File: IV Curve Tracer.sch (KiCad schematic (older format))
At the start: 61 parts, among them IC1 MAX680ESA+, J0 TB002-500-02BE, J1 CAN_Out, J5 Conn_01x15, J6 Conn_01x15, Q1 IRF100P218XKMA1, Q2 IRF100P218XKMA1, SW0 SW_Rotary2x3, U1 INA211CQDCKRQ1, U2 LT1215, U3 LT1215, U4 ADM3055E, U5 CDSOT23-T24CAN

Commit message: CAN updated, needs bugfixes and footprint review.
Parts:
- added C18, C3: .1uF, Capacitor_SMD:C_0402_1005Metric, symbol IV-Curve-Tracer-rescue:SMDTC04100TA00JS00-SamacSys_Parts-IV-Curve-Tracer-rescue
- added J7: CAN_In, TerminalBlock_Phoenix:TerminalBlock_Phoenix_MKDS-1,5-4_1x04_P5.00mm_Horizontal, symbol Connector:Screw_Terminal_01x04
- added TP10: CAN_Rx, TestPoint:TestPoint_Keystone_5005-5009_Compact, symbol Connector:TestPoint
- added TP11: CAN_Tx, TestPoint:TestPoint_Keystone_5005-5009_Compact, symbol Connector:TestPoint
- added TP12: GroundTP, TestPoint:TestPoint_Keystone_5005-5009_Compact, symbol Connector:TestPoint
- added TP6: ISO_Vout, TestPoint:TestPoint_Keystone_5005-5009_Compact, symbol Connector:TestPoint
- added TP7: ISO_Vin, TestPoint:TestPoint_Keystone_5005-5009_Compact, symbol Connector:TestPoint
- added TP8: ISO_GNDout, TestPoint:TestPoint_Keystone_5005-5009_Compact, symbol Connector:TestPoint
- added TP9: ISO_GNDin, TestPoint:TestPoint_Keystone_5005-5009_Compact, symbol Connector:TestPoint
- C14, C15, C16, C17: symbol IV-Curve-Tracer-rescue:HMK325C7475KM-PE-SamacSys_Parts -> IV-Curve-Tracer-rescue:HMK325C7475KM-PE-SamacSys_Parts-IV-Curve-Tracer-rescue
- C2, C4, C5: symbol IV-Curve-Tracer-rescue:SMDTC04100TA00JS00-SamacSys_Parts -> IV-Curve-Tracer-rescue:SMDTC04100TA00JS00-SamacSys_Parts-IV-Curve-Tracer-rescue
- IC1: symbol IV-Curve-Tracer-rescue:MAX680ESA+-SamacSys_Parts -> IV-Curve-Tracer-rescue:MAX680ESA+-SamacSys_Parts-IV-Curve-Tracer-rescue
- LED1, LED2, LED3, LED4: symbol IV-Curve-Tracer-rescue:TLHR5400-AS12Z-SamacSys_Parts -> IV-Curve-Tracer-rescue:TLHR5400-AS12Z-SamacSys_Parts-IV-Curve-Tracer-rescue
- SW0: symbol IV-Curve-Tracer-rescue:SW_Rotary2x3-Switch -> IV-Curve-Tracer-rescue:SW_Rotary2x3-Switch-IV-Curve-Tracer-rescue
- U4: symbol IV-Curve-Tracer-rescue:ADM3055EBRIZ-SamacSys_Parts -> IV-Curve-Tracer-rescue:ADM3055EBRIZ-SamacSys_Parts-IV-Curve-Tracer-rescue
- U5: footprint SamacSys_Parts:SOT95P230X117-3N -> Package_TO_SOT_SMD:SOT-23W_Handsoldering; symbol IV-Curve-Tracer-rescue:CDSOT23-T24CAN-SamacSys_Parts -> IV-Curve-Tracer-rescue:CDSOT23-T24CAN-SamacSys_Parts-IV-Curve-Tracer-rescue
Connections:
- wire segments 189 -> 207
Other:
- moved on the sheet: C7, C8, C9

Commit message: proof checked, drc run and mounting holes added.
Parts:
- added H1, H2, H3, H4: MountingHole, MountingHole:MountingHole_3.2mm_M3, symbol Mechanical:MountingHole
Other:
- note added: "CAN Circuit"
- note removed: "* Make a custom \nfootprint for this"

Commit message: moved ADC_V pin down two
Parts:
- J1, J7: footprint TerminalBlock_Phoenix:TerminalBlock_Phoenix_MKDS-1,5-4_1x04_P5.00mm_Horizontal -> Connector_Molex:Molex_Micro-Fit_3.0_43650-0415_1x04_P3.00mm_Vertical
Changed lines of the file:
@@
 	-1   0    0    -1
 $EndComp
-Text GLabel 10900 3900 2    50   Input ~ 0
+Text GLabel 10900 4100 2    50   Input ~ 0
 ADC_V
 Wire Wire Line
@@
 NoConn ~ 10500 4400
 NoConn ~ 10500 4300
-NoConn ~ 10500 4100
+NoConn ~ 10500 3900
 NoConn ~ 10500 3700
 Text Notes 7000 6800 0    50   ~ 0
@@
 	1    0    0    -1
 $EndComp
+$Comp
+L Device:R R8
+U 1 1 5EF5A814
+P 1700 2450
+F 0 "R8" H 1770 2496 50  0000 L CNN
+F 1 "2k" H 1770 2405 50  0000 L CNN
+F 2 "Resistor_THT:R_Axial_DIN0204_L3.6mm_D1.6mm_P5.08mm_Vertical" V 1630 2450 50  0001 C CNN
+F 3 "~" H 1700 2450 50  0001 C CNN
+	1    1700 2450
+	1    0    0    -1
+$EndComp
+Connection ~ 1700 2300
 Connection ~ 1350 2200
 Wire Wire Line
@@
 F 0 "J1" H 8000 5800 60  0000 C CNN
 F 1 "CAN_Out" H 7900 6100 60  0000 C CNN
-F 2 "TerminalBlock_Phoenix:TerminalBlock_Phoenix_MKDS-1,5-4_1x04_P5.00mm_Horizontal" H 8050 6150 60  0001 C CNN
+F 2 "Connector_Molex:Molex_Micro-Fit_3.0_43650-0415_1x04_P3.00mm_Vertical" H 8050 6150 60  0001 C CNN
 F 3 "https://www.mouser.com/datasheet/2/324/3/ItemDetail_1718605-916253.pdf" H 8050 6150 60  0001 C CNN
 	1    7900 5850
@@
 F 0 "J7" H 8000 5200 60  0000 C CNN
 F 1 "CAN_In" H 7900 5500 60  0000 C CNN
-F 2 "TerminalBlock_Phoenix:TerminalBlock_Phoenix_MKDS-1,5-4_1x04_P5.00mm_Horizontal" H 8050 5550 60  0001 C CNN
+F 2 "Connector_Molex:Molex_Micro-Fit_3.0_43650-0415_1x04_P3.00mm_Vertical" H 8050 5550 60  0001 C CNN
 F 3 "https://www.mouser.com/datasheet/2/324/3/ItemDetail_1718605-916253.pdf" H 8050 5550 60  0001 C CNN
 	1    7900 5250
@@
 	10850 4300 10850 3800
 Wire Wire Line
-	10500 3900 10900 3900
+	10500 4100 10900 4100
 Wire Wire Line
 	10500 4000 10900 4000
@@
 Text Notes 850  4700 0    50   ~ 0
 CAN Circuit
-Connection ~ 1700 2300
-$Comp
-L Device:R R8
-U 1 1 5EF5A814
-P 1700 2450
-F 0 "R8" H 1770 2496 50  0000 L CNN
-F 1 "2k" H 1770 2405 50  0000 L CNN
-F 2 "Resistor_THT:R_Axial_DIN0204_L3.6mm_D1.6mm_P5.08mm_Vertical" V 1630 2450 50  0001 C CNN
-F 3 "~" H 1700 2450 50  0001 C CNN
-	1    1700 2450
-	1    0    0    -1
-$EndComp
 $EndSCHEMATC

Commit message: Major Curve Tracer Board overhaul. Schematic advanced to Rev 1.1.0. Layout advanced to Rev 1.1.0. Parts list advanced to Rev 1.1.0.
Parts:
- removed C1: Variable, Capacitor_SMD:C_0805_2012Metric, symbol Device:C
- removed C14, C16, C17: 4.7uF, Capacitor_SMD:C_1210_3225Metric, symbol IV-Curve-Tracer-rescue:HMK325C7475KM-PE-SamacSys_Parts-IV-Curve-Tracer-rescue
- removed C18, C2, C3: .1uF, Capacitor_SMD:C_0402_1005Metric, symbol IV-Curve-Tracer-rescue:SMDTC04100TA00JS00-SamacSys_Parts-IV-Curve-Tracer-rescue
- removed J1: CAN_Out, Connector_Molex:Molex_Micro-Fit_3.0_43650-0415_1x04_P3.00mm_Vertical, symbol Connector:Screw_Terminal_01x04
- removed J5, J6: Conn_01x15, Connector_PinHeader_2.54mm:PinHeader_1x15_P2.54mm_Vertical, symbol Connector_Generic:Conn_01x15
- removed J7: CAN_In, Connector_Molex:Molex_Micro-Fit_3.0_43650-0415_1x04_P3.00mm_Vertical, symbol Connector:Screw_Terminal_01x04
- removed JP1: Termination Resistors, Connector_PinHeader_2.54mm:PinHeader_1x02_P2.54mm_Vertical, symbol Device:Jumper_NC_Small
- removed LED2, LED3, LED4: TLHR5400-AS12Z, LED_THT:LED_D3.0mm, symbol IV-Curve-Tracer-rescue:TLHR5400-AS12Z-SamacSys_Parts-IV-Curve-Tracer-rescue
- removed R10, R9: 330, Resistor_THT:R_Axial_DIN0204_L3.6mm_D1.6mm_P5.08mm_Vertical, symbol Device:R
- removed R11: 1k, Resistor_THT:R_Axial_DIN0204_L3.6mm_D1.6mm_P5.08mm_Vertical, symbol Device:R
- removed R12: 0, Resistor_SMD:R_0805_2012Metric, symbol Device:R
- removed R14, R15: 60, Resistor_SMD:R_0805_2012Metric, symbol Device:R
- removed TP4: CAN_H, TestPoint:TestPoint_Keystone_5005-5009_Compact, symbol Connector:TestPoint
- removed TP5: CAN_L, TestPoint:TestPoint_Keystone_5005-5009_Compact, symbol Connector:TestPoint
- removed TP6: ISO_Vout, TestPoint:TestPoint_Keystone_5005-5009_Compact, symbol Connector:TestPoint
- removed U5: CDSOT23-T24CAN, Package_TO_SOT_SMD:SOT-23W_Handsoldering, symbol IV-Curve-Tracer-rescue:CDSOT23-T24CAN-SamacSys_Parts-IV-Curve-Tracer-rescue
- added C0, C15: .1uF, Capacitor_SMD:C_0805_2012Metric, symbol Device:C_Small
- added C14: 10uF, Capacitor_SMD:C_0805_2012Metric, symbol Device:C_Small
- added C16, CA_2, CB_2, CC_2: .01uF, Capacitor_SMD:C_0805_2012Metric, symbol Device:C_Small
- added C5: 4.7uF, Capacitor_SMD:C_0805_2012Metric, symbol Device:C_Small
- added F1: Fuse, IV Curve Tracer:05200101Z_Fuze_Holder_5x20_PCB_Mount, symbol Device:Fuse
- added J0: 9V Supply, Connector_Molex:Molex_Micro-Fit_3.0_43650-0215_1x02_P3.00mm_Vertical, symbol Connector_Generic:Conn_01x02
- added J2: CAN_In, Connector_Molex:Molex_Micro-Fit_3.0_43650-0415_1x04_P3.00mm_Vertical, symbol Array:CAN_Connector_43650-0427
- added J3: CAN_Out, Connector_Molex:Molex_Micro-Fit_3.0_43650-0415_1x04_P3.00mm_Vertical, symbol Array:CAN_Connector_43650-0427
- added JP1: Termination Resistors, Connector_PinHeader_2.54mm:PinHeader_1x02_P2.54mm_Vertical, symbol Device:Jumper_NO_Small
- added LED2: Scanning (Blue), LED_SMD:LED_0805_2012Metric, symbol Device:LED_ALT
- added LED3: CAN_Rx (Blue), LED_SMD:LED_0805_2012Metric, symbol Device:LED_ALT
- added LED4: CAN_Tx (Blue), LED_SMD:LED_0805_2012Metric, symbol Device:LED_ALT
- added LED5: Error (Amber), LED_SMD:LED_0805_2012Metric, symbol Device:LED_ALT
- added R1, R2, R3, R5: 330, Resistor_SMD:R_0805_2012Metric, symbol Device:R
- added R16: 0, Resistor_SMD:R_0805_2012Metric, symbol Device:R_Small
- added R17, R18: 60, Resistor_SMD:R_0805_2012Metric, symbol Device:R_Small
- added SW1: SW_Push, Button_Switch_THT:SW_PUSH_6mm, symbol Switch:SW_Push
- added TP1: GND, TestPoint:TestPoint_Keystone_5005-5009_Compact, symbol Connector:TestPoint
- added TP12: CAN_ISO_GndOut, TestPoint:TestPoint_Keystone_5005-5009_Compact, symbol Connector:TestPoint
- added TP13: CAN_H, TestPoint:TestPoint_Keystone_5005-5009_Compact, symbol Connector:TestPoint
- added TP14: CAN_L, TestPoint:TestPoint_Keystone_5005-5009_Compact, symbol Connector:TestPoint
- added U1: MCU_Nucleo_L432KC, IV Curve Tracer:MODULE_NUCLEO-L432KC, symbol Array:MCU_Nucleo_L432KC
- added U7: CDSOT23-T24CAN, Package_TO_SOT_SMD:SOT-23, symbol Array:CAN_Bus_Protector_CDSOT23-T24CAN
- C1: renamed from C4; footprint Capacitor_SMD:C_0402_1005Metric -> Capacitor_SMD:C_0805_2012Metric; symbol IV-Curve-Tracer-rescue:SMDTC04100TA00JS00-SamacSys_Parts-IV-Curve-Tracer-rescue -> Device:C_Small; Description CGA2B1X7R1C104K050BC - Multilayer Ceramic Capacitors MLCC -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 -> (none)
- C10: value 0.22uF -> .1uF
- C11: value 10uF -> .1uF
- C12: value 0.1uF -> .01uF
- C13: value 0.01uF -> .22uF
- C3: renamed from C5; footprint Capacitor_SMD:C_0402_1005Metric -> Capacitor_SMD:C_0805_2012Metric; symbol IV-Curve-Tracer-rescue:SMDTC04100TA00JS00-SamacSys_Parts-IV-Curve-Tracer-rescue -> Device:C_Small; Description CGA2B1X7R1C104K050BC - Multilayer Ceramic Capacitors MLCC -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 -> (none)
- C4: renamed from C15; footprint Capacitor_SMD:C_1210_3225Metric -> Capacitor_SMD:C_0805_2012Metric; symbol IV-Curve-Tracer-rescue:HMK325C7475KM-PE-SamacSys_Parts-IV-Curve-Tracer-rescue -> Device:C_Small; Description HMK325C7475KM-PE - Multilayer Ceramic Capacitors MLCC - SMD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 -> (none)
- C6: value 10uF -> 4.7uF; Height (none) -> 2.7; Manufacturer_Name (none) -> TAIYO YUDEN; Manufacturer_Part_Number (none) -> HMK325C7475KM-PE; Mouser Part Number (none) -> 963-HMK325C7475KM-PE; Mouser Price/Stock (none) -> https://www.mouser.co.uk/ProductDetail/Taiyo-Yuden/HMK325C7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
- C7: value 0.1uF -> 4.7uF; Height (none) -> 2.7; Manufacturer_Name (none) -> TAIYO YUDEN; Manufacturer_Part_Number (none) -> HMK325C7475KM-PE; Mouser Part Number (none) -> 963-HMK325C7475KM-PE; Mouser Price/Stock (none) -> https://www.mouser.co.uk/ProductDetail/Taiyo-Yuden/HMK325C7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
- C8: value 0.1uF -> .1uF; Height (none) -> 5; Manufacturer_Name (none) -> WIMA; Manufacturer_Part_Number (none) -> SMDTC04100TA00JS00; Mouser Part Number (none) -> 505-SMDTC04100TA00JS; Mouser Price/Stock (none) -> https://www.mouser.co.uk/ProductDetail/WIMA/SMDTC04100TA00J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
- C9: value 0.01uF -> 10uF
- D1: value 1N5226B-B -> 3.9V Zener; footprint Diode_THT:D_DO-35_SOD27_P7.62mm_Horizontal -> Diode_SMD:D_0805_2012Metric; symbol Device:D_Zener -> Device:D_Zener_ALT
- J1: renamed from J0; value TB002-500-02BE -> Solar Array; footprint IV Curve Tracer:ExpandedBlockTerminal-2H_P7.62mm -> IV Curve Tracer:PhoenixContact_PowerCombicon5_GF_2x7.62mm; symbol Connector:Screw_Terminal_01x02 -> Array:PWR_Connector_1720796; Description Fixed Terminal Blocks screw type, 5.00, horizontal, 2 poles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 -> (none)
- L1, L2: value 2kH -> 1.8kH
- LED1: value TLHR5400-AS12Z -> Heartbeat (Blue); footprint LED_THT:LED_D3.0mm -> LED_SMD:LED_0805_2012Metric; symbol IV-Curve-Tracer-rescue:TLHR5400-AS12Z-SamacSys_Parts-IV-Curve-Tracer-rescue -> Device:LED_ALT; Description Standard LEDs - Through Hole Red 10mcd; 5mm 612-625nm; 2V T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 -> (none)
- R10: renamed from R2; footprint Resistor_THT:R_Axial_DIN0204_L3.6mm_D1.6mm_P5.08mm_Vertical -> Resistor_SMD:R_0805_2012Metric
- R11: renamed from R5; value R5: RN732BTTD56R6F50 (56.6k) -> 56.6k; footprint Resistor_SMD:R_1206_3216Metric_Pad1.42x1.75mm_HandSolder -> Resistor_SMD:R_0805_2012Metric
- R12: renamed from R6; footprint Resistor_THT:R_Axial_DIN0204_L3.6mm_D1.6mm_P5.08mm_Vertical -> Resistor_SMD:R_0805_2012Metric
- R13: renamed from R7; value R7: RN73H2BTTD1323F25 (132kO) -> 132k; footprint Resistor_SMD:R_1206_3216Metric -> Resistor_SMD:R_0805_2012Metric
- R14: renamed from R8; footprint Resistor_THT:R_Axial_DIN0204_L3.6mm_D1.6mm_P5.08mm_Vertical -> Resistor_SMD:R_0805_2012Metric
- R15: renamed from R3; value R3: WSLF2512L5000FEB (.5mO) -> .5m
- R4: footprint Resistor_THT:R_Axial_DIN0204_L3.6mm_D1.6mm_P5.08mm_Vertical -> Resistor_SMD:R_0805_2012Metric
- R6: renamed from Ri1; footprint Resistor_THT:R_Axial_DIN0204_L3.6mm_D1.6mm_P5.08mm_Vertical -> Resistor_SMD:R_0805_2012Metric
- R7: renamed from R1; footprint Resistor_THT:R_Axial_DIN0204_L3.6mm_D1.6mm_P5.08mm_Vertical -> Resistor_SMD:R_0805_2012Metric
- R8: renamed from Rf1; footprint Resistor_THT:R_Axial_DIN0204_L3.6mm_D1.6mm_P5.08mm_Vertical -> Resistor_SMD:R_0805_2012Metric
- R9: renamed from Rf2; footprint Resistor_THT:R_Axial_DIN0204_L3.6mm_D1.6mm_P5.08mm_Vertical -> Resistor_SMD:R_0805_2012Metric
- SW2: renamed from SW0; value SW_Rotary2x3 -> A20303RNCG; footprint CK1052:CK1052 -> IV Curve Tracer:A20303RNCG_rotary_sw_dp3t; symbol IV-Curve-Tracer-rescue:SW_Rotary2x3-Switch-IV-Curve-Tracer-rescue -> Array:SW_Rotary2x3
- TP10: value CAN_Rx -> CAN_ISO_Vin
- TP11: value CAN_Tx -> CAN_ISO_GndIn
- TP2: renamed from TP0; value TestPoint -> Array Current; footprint TestPoint:TestPoint_Plated_Hole_D2.0mm -> TestPoint:TestPoint_Keystone_5005-5009_Compact
- TP3: renamed from TP1; value TestPoint -> Array Voltage; footprint TestPoint:TestPoint_Plated_Hole_D2.0mm -> TestPoint:TestPoint_Keystone_5005-5009_Compact
- TP4: renamed from TP2; value TestPoint -> +10V; footprint TestPoint:TestPoint_Plated_Hole_D2.0mm -> TestPoint:TestPoint_Keystone_5005-5009_Compact
- TP5: renamed from TP3; value TestPoint -> Gate; footprint TestPoint:TestPoint_Plated_Hole_D2.0mm -> TestPoint:TestPoint_Keystone_5005-5009_Compact
- TP6: renamed from TP12; value GroundTP -> GND
- TP7: value ISO_Vin -> CAN_Tx
- TP8: value ISO_GNDout -> CAN_Rx
- TP9: value ISO_GNDin -> CAN_ISO_Vout
- U2: renamed from U1; value INA211CQDCKRQ1 -> INA211; footprint Package_TO_SOT_SMD:SOT-363_SC-70-6_Handsoldering -> IV Curve Tracer:SC70-6; symbol Array_Curve_Tracer:INA211 -> Array:INA211
- U3: renamed from U2; footprint Package_SO:SO-8_5.3x6.2mm_P1.27mm -> Package_SO:SO-8_3.9x4.9mm_P1.27mm
- U4: renamed from IC1; footprint Package_DIP:DIP-8_W7.62mm_Socket_LongPads -> Package_SO:SOIC-8_3.9x4.9mm_P1.27mm; symbol IV-Curve-Tracer-rescue:MAX680ESA+-SamacSys_Parts-IV-Curve-Tracer-rescue -> Array:MAX681; Description MAX680ESA+, Charge Pump Inverting, Step Up 10mA 8 kHz, +/-1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 -> (none)
- U5: renamed from U3; footprint Package_SO:SO-8_5.3x6.2mm_P1.27mm -> Package_SO:SO-8_3.9x4.9mm_P1.27mm
- U6: renamed from U4; footprint SamacSys_Parts:SOIC127P1030X264-20N -> IV Curve Tracer:ADM3055EBRIZ; symbol IV-Curve-Tracer-rescue:ADM3055EBRIZ-SamacSys_Parts-IV-Curve-Tracer-rescue -> Array:CAN_Chip_ADM3055E
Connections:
- net labels added: +3V3, +9V, +Current_Sense, -Current_Sense, Array_Current, Array_Voltage, CAN_Rx, CAN_Tx, Error, Gate, Heartbeat, Reset, Scanning, Voltage_Sense
- net labels removed: ADC_C, ADC_V, CAN_H, CAN_L, CAN_RX, CAN_TX, GATE, RSlope, TERM_H, TERM_L
- wire segments 207 -> 210
- no-connect marks 28 -> 25
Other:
- note added: "5V to 10V power feeding into MOSFET controller."
- note added: "CAN"
- note added: "CX_2 capacitors are optional and can \nbe left unsoldered. For input filtering."
- note added: "Current Sensor"
- note added: "Gate Amplifier"
- note added: "LEDs"
- note added: "Must be close\nto V_ISO_In\n---------"
- note added: "Must be close\nto V_ISO_Out\n---------"
- note added: "Nucleo Connections"
- note added: "PV Controller"
- note added: "Powered and controlled by USB through STLink UART.\nRequires A7 (PA2) andA2 (PA3) to be reserved."
- note added: "Rev 1.1:\n\nSchematic:\n- Reannotated all component labels and reversed rescued schematic symbols.\n- Rearranged schematic and cleaned up component positioning.\n- Used Array.lib for array-relevant schematic symbols.\n- Standardized components lists.\n- Added fuse to array input and swapped to a phoenix connector.\n- Updated indicator LEDs and added Reset button.\n- Added connector for 9V power s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"
- note added: "Status LEDs for\nat-a-glance\ninformation."
- note added: "This is really complicated.\nI blame Analog Devices."
- note added: "Voltage Sensor"
- note removed: "* Footprint for this \nmight be a little big"
- note removed: "* Might be 3.9k, or 3.9k \nchained to 100 ohm"
- note removed: "1"
- note removed: "6/22/20"
- note removed: "As long as total equals to 120 Ohms,\nthe two termination resistors can be any value"
- note removed: "CAN Bus\nProtection"
- note removed: "CAN Circuit"
- note removed: "Current Sensor Op-Amp"
- note removed: "DAC to control MOSFET"
- note removed: "IV Curve Tracer PCB"
- note removed: "Must be close\nto V_ISO_In"
- note removed: "Must be close\nto V_ISO_Out"
- note removed: "Powered\nBy USB\n"
- note removed: "Voltage Sensor Op-Amp"
- note removed: "Youssef Elsherif\nGary Hallock\nMatthew Yu"
- moved on the sheet: H1, H2, H3, H4, HS1, Q1, Q2, R10, R11, R12, R13, R14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

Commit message: Addressed review.
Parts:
- removed C1, C8: .1uF, Capacitor_SMD:C_0805_2012Metric, symbol Device:C_Small
- removed U2: INA211, IV Curve Tracer:SC70-6, symbol Array:INA211
- removed U5: LT1215, Package_SO:SO-8_3.9x4.9mm_P1.27mm, symbol Amplifier_Operational:LT1492
- added C2: 0.1uF, Capacitor_SMD:C_0805_2012Metric, symbol Device:C_Small
- added C3: 1uF, Capacitor_SMD:C_0805_2012Metric, symbol Device:C_Small
- added D1: 3.9V Zener, Diode_SMD:D_SOD-123F, symbol Device:D_Zener_Small_ALT
- added D2: Diode, Diode_SMD:D_SOD-123F, symbol Device:D_Small_ALT
- added D4: Diode, Diode_SMD:D_SOD-123F, symbol Device:D_ALT
- added R7: 1.7k, Resistor_SMD:R_0805_2012Metric, symbol Device:R_Small
- added TP1: 9V, TestPoint:TestPoint_Keystone_5005-5009_Compact, symbol Connector:TestPoint
- added U2: INA210, IV Curve Tracer:SC70-6, symbol Array:OP_AMP_INA21x
- C1: renamed from C0; value .1uF -> 0.1uF
- C4: renamed from CA_2; value .01uF -> 1uF
- C5: renamed from CB_2; value .01uF -> 0.1uF
- C6: renamed from CC_2; value .01uF -> 0.01uF
- C7: renamed from C3; value .1uF -> 0.1uF
- D3: renamed from D1; footprint Diode_SMD:D_0805_2012Metric -> Diode_SMD:D_SOD-123F
- R6: renamed from R15; value .5m -> 2m; footprint IV Curve Tracer:R-WSLF2512L5000FEB -> Resistor_SMD:R_1206_3216Metric
- TP3: renamed from TP2; value Array Current -> Array_I
- renumbered C6 to C10, C7 to C11, C9 to C12, C10 to C13, C11 to C14, C12 to C15, C13 to C16, C14 to C17, C15 to C18, C16 to C19, C4 to C8, C5 to C9, J0 to J1, J1 to J2, J2 to J3, J3 to J4, R8 to R10, R9 to R11, R10 to R12, R11 to R13, R12 to R14, R13 to R15, R14 to R16, R16 to R17, R17 to R18, R18 to R19, R6 to R8, R7 to R9, TP9 to TP10, TP10 to TP11, TP11 to TP12, TP12 to TP13, TP13 to TP14, TP14 to TP15, TP1 to TP2, TP3 to TP4, TP4 to TP5, TP5 to TP6, TP6 to TP7, TP7 to TP8, TP8 to TP9, U6 to U5, U7 to U6
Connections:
- net +10V: now also C7.2, U3.8 (V+)
- net +3V3: no longer C7.2, U3.8 (V+)
- net +9V: now also C2.2, TP1.1, U2.3 (V+)
- net +Current_Sense: now also U2.4 (+)
- net Array_Current: now also C3.1, D1.1 (K), D2.1 (K), R7.1
- net Array_Voltage: now also D3.1 (K), D4.1 (K)
- net DAC_Control: now also U1.22 (A3), U3.5 (+); no longer U1.20 (A1)
- net GND: now also C2.1, C3.2, D1.2 (A), D2.2 (A), D4.2 (A), U2.1 (REF), U2.2 (V-), U2.5 (-)
- net Gate: now also U3.7
- net at C4.1, C5.1, C6.1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: no longer D3.1 (K)
- net at R11.2, R12.1: now also U3.6 (-)
- new net: R7.2, U2.6
- no-connect marks 25 -> 19
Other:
- note added: "CX_2 capacitors are optional \nand can be left unsoldered. \nFor input filtering."
- note added: "Powered and controlled by USB through STLink UART.\nRequires A7 (PA2) and A2 (PA3) to be reserved."
- note added: "Rev 1.1:\n\nSchematic:\n- Reannotated all component labels and reversed rescued schematic symbols.\n- Rearranged schematic and cleaned up component positioning.\n- Used Array.lib for array-relevant schematic symbols.\n- Standardized components lists.\n- Added fuse to array input and swapped to a phoenix connector.\n- Updated indicator LEDs and added Reset button.\n- Standardized current sensor to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"
- note removed: "CX_2 capacitors are optional and can \nbe left unsoldered. For input filtering."
- note removed: "Powered and controlled by USB through STLink UART.\nRequires A7 (PA2) andA2 (PA3) to be reserved."
- note removed: "Rev 1.1:\n\nSchematic:\n- Reannotated all component labels and reversed rescued schematic symbols.\n- Rearranged schematic and cleaned up component positioning.\n- Used Array.lib for array-relevant schematic symbols.\n- Standardized components lists.\n- Added fuse to array input and swapped to a phoenix connector.\n- Updated indicator LEDs and added Reset button.\n- Added connector for 9V power s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"
- moved on the sheet: C4, C5, C6, C7, D3, LED1, LED2, LED3, LED4, LED5, R1, R10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

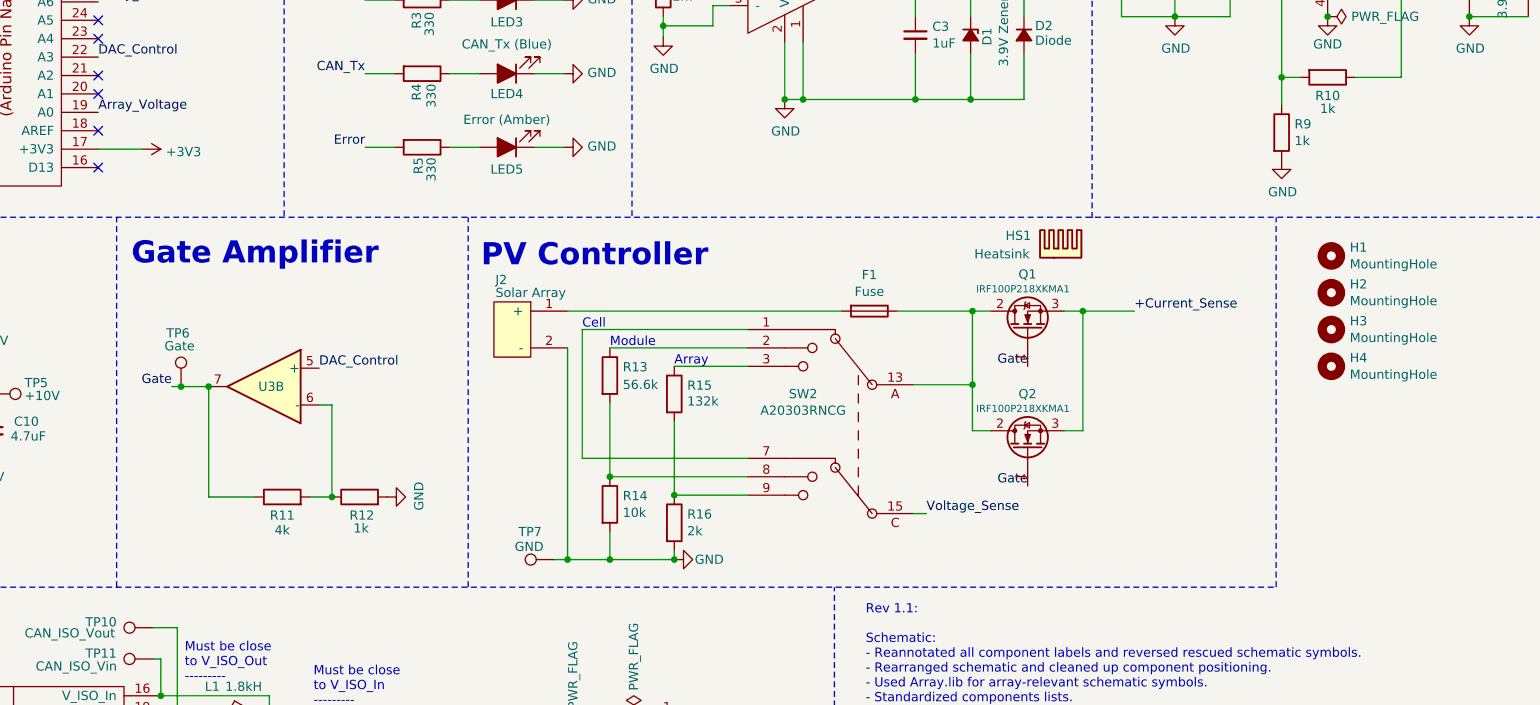
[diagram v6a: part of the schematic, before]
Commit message: added bodge notes to current version Curve Tracer
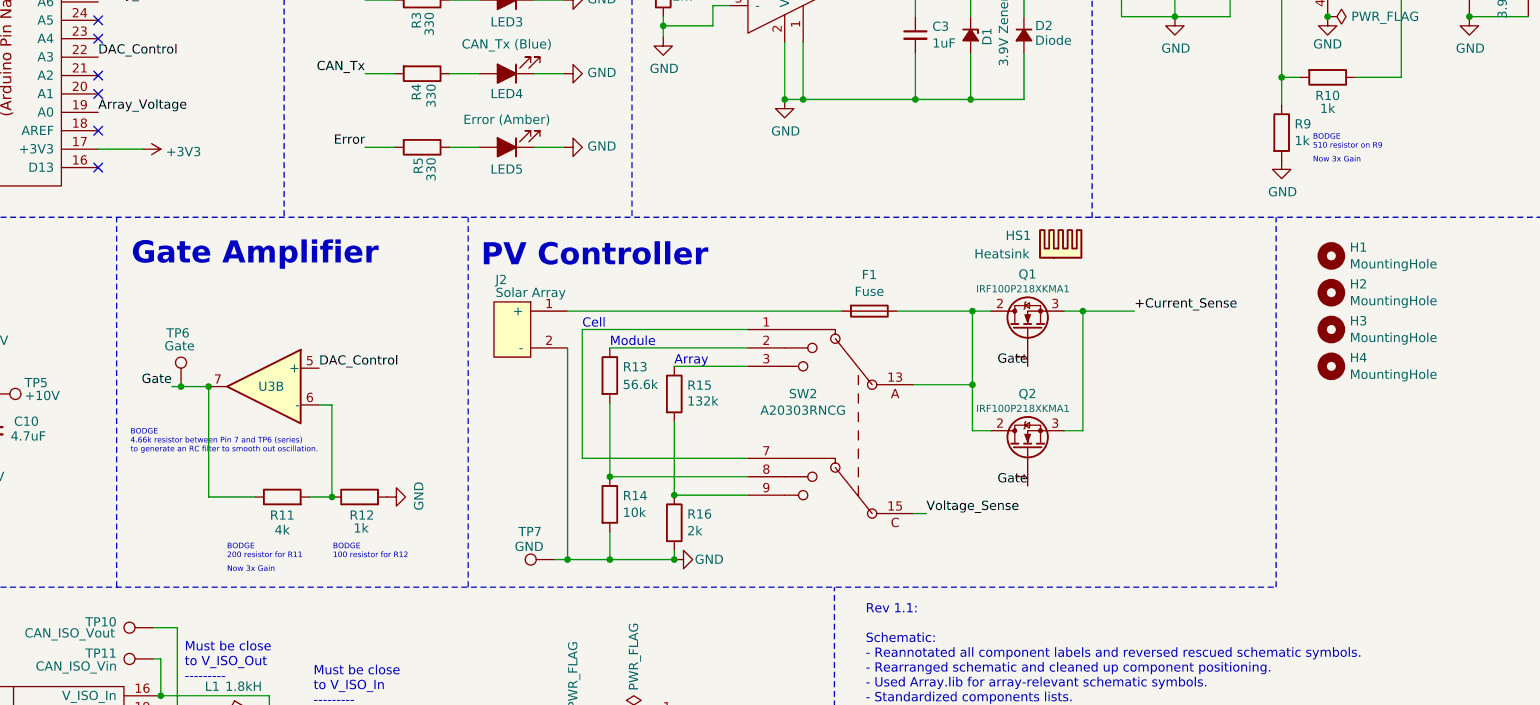
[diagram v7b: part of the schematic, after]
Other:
- note added: "BODGE\n100 resistor for R12"
- note added: "BODGE\n200 resistor for R11"
- note added: "BODGE\n4.66k resistor between Pin 7 and TP6 (series) \nto generate an RC filter to smooth out oscillation."
- note added: "BODGE\n510 resistor on R9"
- note added: "Now 3x Gain"
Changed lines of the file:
@@
 $EndComp
 Connection ~ 2910 1320
+Text Notes 2975 4375 0    30   ~ 0
+BODGE\n4.66k resistor between Pin 7 and TP6 (series) \nto generate an RC filter to smooth out oscillation.
+Text Notes 3500 4950 0    30   ~ 0
+BODGE\n200 resistor for R11
+Text Notes 4075 4950 0    30   ~ 0
+BODGE\n100 resistor for R12
+Text Notes 9400 2725 0    30   ~ 0
+BODGE\n510 resistor on R9
+Text Notes 9400 2800 0    30   ~ 0
+Now 3x Gain
+Text Notes 3500 5025 0    30   ~ 0
+Now 3x Gain
 $EndSCHEMATC
